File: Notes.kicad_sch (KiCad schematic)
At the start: 0 parts

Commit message: Updated notes
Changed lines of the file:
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@@
 		)
 	)
-	(text_box "POWER MANAGEMENT NOTES:\n- The input power goes through three stages \n  1. a) External Power: LM73100RPWR, 2.7 - 23 V, 5.5 A Integrated Ideal Diode with Input Reverse Polarity and Overvoltage Protection\n     b) USB POWER: SS34-E3/57T Diode\n  2. TPS259531DSGR 2.7V to 18V, 4-A, 34-mΩ eFuse With Fast Overvoltage Protection\n  3. TPS62442RQRR, 2.75-V to 6-V, Dual-Channel Step-Down Converter with Adjustable Frequency\n\n- Stage Description:\n  1. The power is sourced from the imediatelly connected power source without relying on jumpers to manual selection. The diodes prevent current from flowing back to a source in case of multiple ppower sources being conected.\n     The ideal diode was used for thhe external power source to limit power loss inherent in a regular diode as the eternal power source will at times be a battery.   \n     The ideal diode includes ppolarity protection (not required on the USB sources)\n  2. The eFuse provides overvoltage protection, undervoltage lockout, and limits inrussh current.\n  3. SMPS that outputs two power rails. The first is dedicated and controlled by the ESP32P4 core. The second is general 3.3V power rail used by all other components.\n"
+	(text_box "POWER MANAGEMENT NOTES:\n- The input power goes through three stages \n  1. a) External Power: LM73100RPWR, 2.7 - 23 V, 5.5 A Integrated Ideal Diode with Input Reverse Polarity and Overvoltage Protection\n     b) USB POWER: SS34-E3/57T Diode\n  2. TPS259531DSGR 2.7V to 18V, 4-A, 34-mΩ eFuse With Fast Overvoltage Protection\n  3. TPS62442RQRR, 2.75-V to 6-V, Dual-Channel Step-Down Converter with Adjustable Frequency\n\n- Stage Description:\n  1. The power is sourced from the imediatelly connected power source without relying on jumpers to manual selection. The diodes prevent current from flowing back to a source in case of multiple ppower sources being conected.\n     The ideal diode was used for thhe external power source to limit power loss inherent in a regular diode as the eternal power source will at times be a battery.   \n     The ideal diode includes ppolarity protection (not required on the USB sources)\n  2. The eFuse provides overvoltage protection, undervoltage lockout, Short Circuit Protection, and limits inrussh current.\n  3. SMPS that outputs two power rails. The first is dedicated and controlled by the ESP32P4 core. The second is general 3.3V power rail used by all other components.\n"
 		(exclude_from_sim no)
 		(at 27.305 29.845 0)

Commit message: SMA Update
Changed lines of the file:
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@@
 	(generator_version "8.0")
 	(paper "A4")
-	(text_box "INTERFACE NOTES:\n- SPI2 IOMUX, DMA\n- SPI3 GPIOMATRIX, NODMA\n- I2S1 GPIOMATRIX\n- I2S2 GPIOMATRIX\n- I2C0 GPIOMATRIX CSI and P4 to C5\n- I2C1 GPIOMATRIX External Interface\n- UART0 IOMUX DEBUG\n- UART1 IOMUX External Interface\n- UART2\n- UART3\n- UART4\n- I3C\n- PARLIO\n  - PSSI_PDCK (Parallel Data Clock) to parlio_tx_clk_pad_out\n  - PSSI_RDY (Ready / Flow Control) to \n  - PSSI_DE (Data Enable) to parlio_tx_data15_pad_out MSB\n  - PSSI_D0 through PSSI_D7 (8-bit Data Bus) to parlio_tx_data0_pad_out 0 to 7\n  Connect suitable pins to the PSSI/SPI header then setup pins with ESP32P4 signals\n- DSI (LCD)\n  - LCD Choice: CTP ST7701S FT5316 D310FPC9362 CST128 (MIPI 2 LANE)\n- SDIO\n  - HS Communication between the P4 and C5 (Slave)\n  - INT pin deddicated as interrupt from C5 to P4 (Not part of SDIO)\n\nSERIES TERMINATION\n- CSI, DSI, SDIO (near P4), UART0, UART1, NOT I2C\nSDIO\n- Array Series termination on SDIO DATA 0-3\n- Individual series termination on CLK, CMD\n- PU on the SDIO INT (Interrupt) pin (Open Drain)"
+	(text_box "CONTROLLED IMPEDANCE TRACE WIDTHS\n(Simulations done using ADS Controlled Impedance Line Designer)\n- Simulated is JLCPCB: JLC04161H-3313(Finished thickness1.56mm±10%)\n\n1. Microstrip Edge Coupled, 100 Ohm Differential Impedance, 0.35mm (center to center), 50mmm Length, f=1Ghz, Width = 0.1225 mm\n2. Coplanar Edge Coupled, 100 Ohm Differential Impedance, 0.35mm (center to center), 0.25mm Clearance, 50mmm Length, f=1Ghz, Width = 0.1354 mm\n3. USB Coplanar Edge Coupled, 90 Ohm Differential Impedance, 0.5mm (center to center), 0.25mm Clearance, 50mmm Length, f=240Mhz, Width = 0.1704 mm\n4. USB Microstrip Edge Coupled, 90 Ohm Differential Impedance, 0.5mm (center to center), 50mmm Length, f=240Mhz, Width = 0.1722 mm\n\nSMA CONNECTOR SIGNAL PIN (MIDDLE) FOOTPRINT\n- With normal 0.35 mm clearance resulted in a veryy significant signal degradation\n- I recalculated the clearance for the middle pin using ADS:\n  - Coplanar Single-Ended, Length: 5mm, Width: 1.37 mmm (width of the pin), f: 5GHz, Clearance = 0.4046 mm\n  \n\nINTERFACE NOTES:\n- SPI2 IOMUX, DMA\n- SPI3 GPIOMATRIX, NODMA\n- I2S1 GPIOMATRIX\n- I2S2 GPIOMATRIX\n- I2C0 GPIOMATRIX CSI and P4 to C5\n- I2C1 GPIOMATRIX External Interface\n- UART0 IOMUX DEBUG\n- UART1 IOMUX External Interface\n- UART2\n- UART3\n- UART4\n- I3C\n- PARLIO\n  - PSSI_PDCK (Parallel Data Clock) to parlio_tx_clk_pad_out\n  - PSSI_RDY (Ready / Flow Control) to \n  - PSSI_DE (Data Enable) to parlio_tx_data15_pad_out MSB\n  - PSSI_D0 through PSSI_D7 (8-bit Data Bus) to parlio_tx_data0_pad_out 0 to 7\n  Connect suitable pins to the PSSI/SPI header then setup pins with ESP32P4 signals\n- DSI (LCD)\n  - LCD Choice: CTP ST7701S FT5316 D310FPC9362 CST128 (MIPI 2 LANE)\n- SDIO\n  - HS Communication between the P4 and C5 (Slave)\n  - INT pin deddicated as interrupt from C5 to P4 (Not part of SDIO)\n\nSERIES TERMINATION\n- CSI, DSI, SDIO (near P4), UART0, UART1, NOT I2C\nSDIO\n- Array Series termination on SDIO DATA 0-3\n- Individual series termination on CLK, CMD\n- PU on the SDIO INT (Interrupt) pin (Open Drain)"
 		(exclude_from_sim no)
 		(at 113.03 29.464 0)

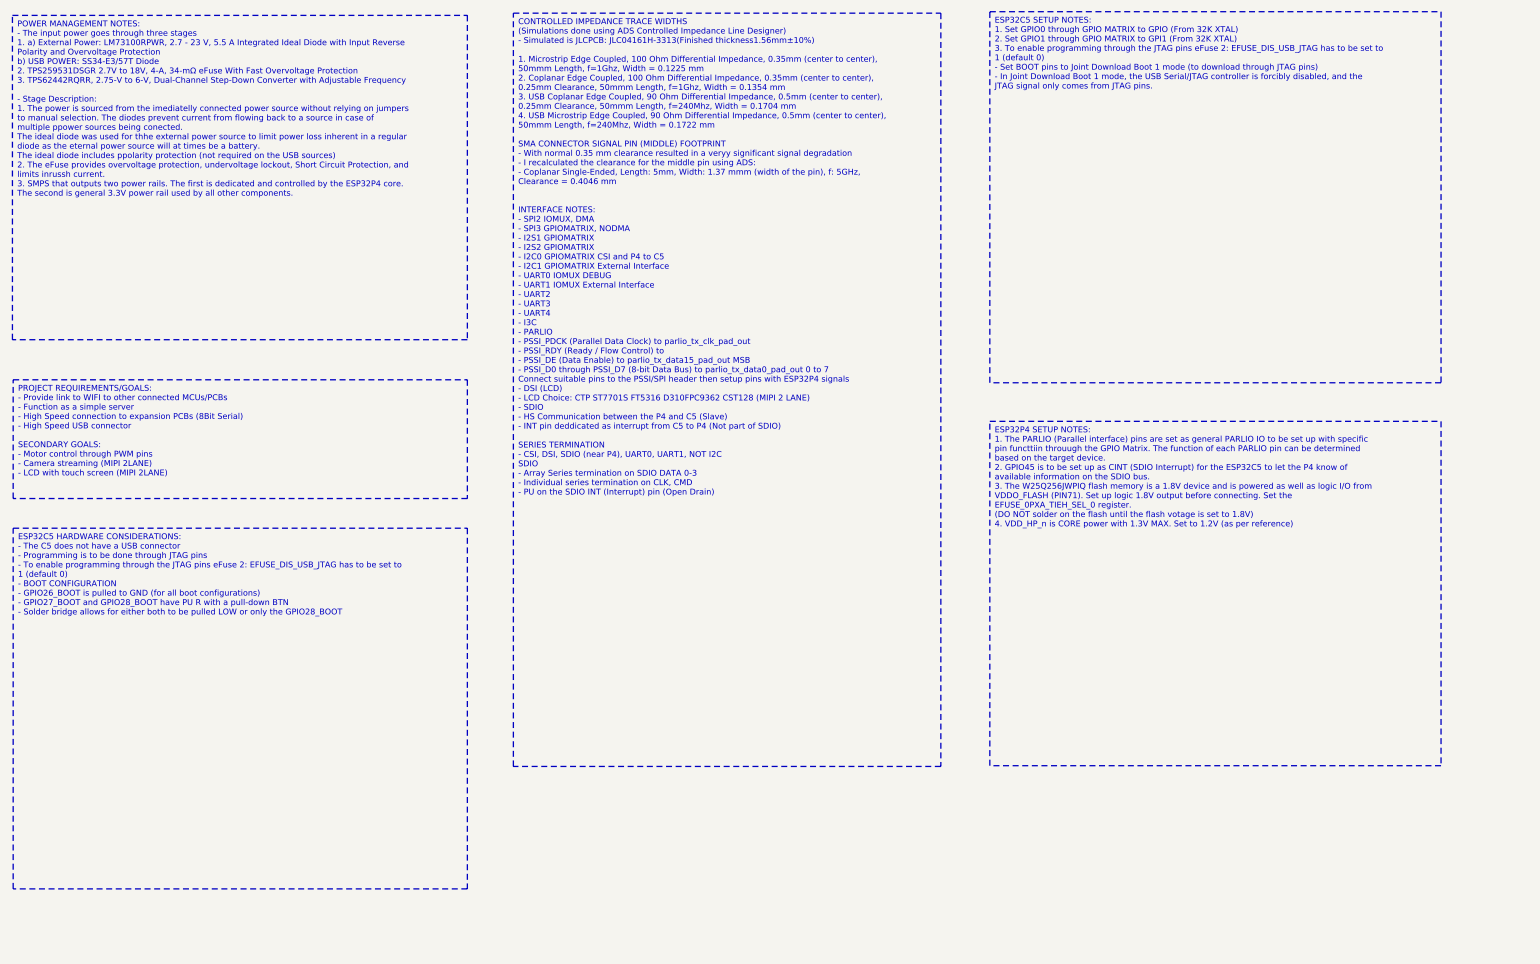
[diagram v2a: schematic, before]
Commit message: QSPI Memory Bus
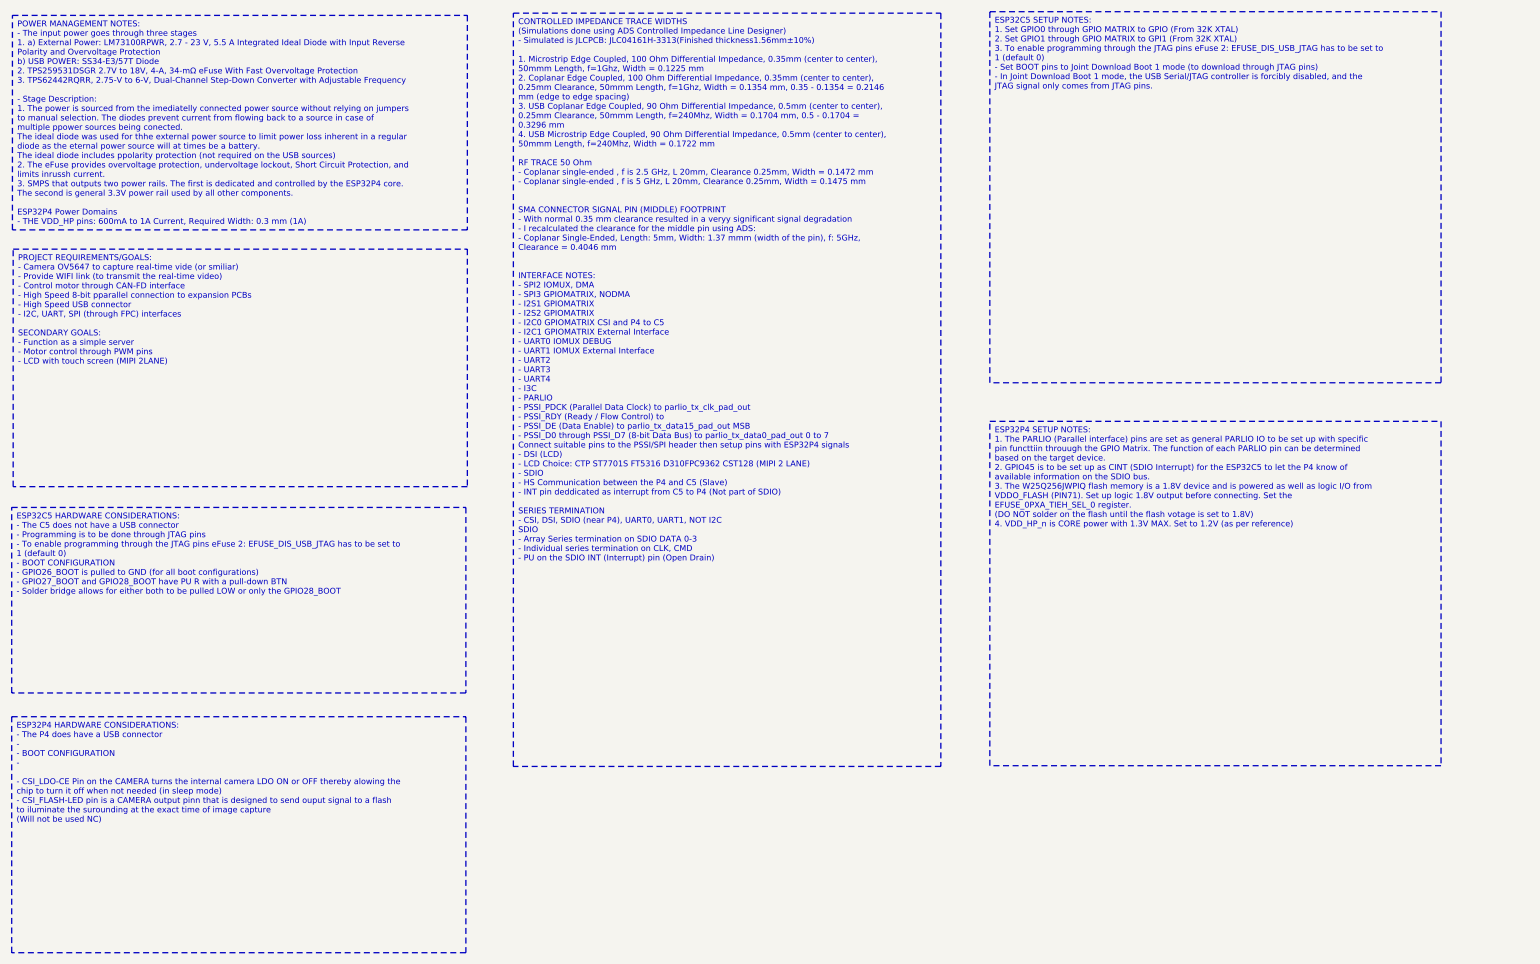
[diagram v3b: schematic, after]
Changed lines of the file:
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@@
 	(generator_version "8.0")
 	(paper "A4")
-	(text_box "CONTROLLED IMPEDANCE TRACE WIDTHS\n(Simulations done using ADS Controlled Impedance Line Designer)\n- Simulated is JLCPCB: JLC04161H-3313(Finished thickness1.56mm±10%)\n\n1. Microstrip Edge Coupled, 100 Ohm Differential Impedance, 0.35mm (center to center), 50mmm Length, f=1Ghz, Width = 0.1225 mm\n2. Coplanar Edge Coupled, 100 Ohm Differential Impedance, 0.35mm (center to center), 0.25mm Clearance, 50mmm Length, f=1Ghz, Width = 0.1354 mm\n3. USB Coplanar Edge Coupled, 90 Ohm Differential Impedance, 0.5mm (center to center), 0.25mm Clearance, 50mmm Length, f=240Mhz, Width = 0.1704 mm\n4. USB Microstrip Edge Coupled, 90 Ohm Differential Impedance, 0.5mm (center to center), 50mmm Length, f=240Mhz, Width = 0.1722 mm\n\nSMA CONNECTOR SIGNAL PIN (MIDDLE) FOOTPRINT\n- With normal 0.35 mm clearance resulted in a veryy significant signal degradation\n- I recalculated the clearance for the middle pin using ADS:\n  - Coplanar Single-Ended, Length: 5mm, Width: 1.37 mmm (width of the pin), f: 5GHz, Clearance = 0.4046 mm\n  \n\nINTERFACE NOTES:\n- SPI2 IOMUX, DMA\n- SPI3 GPIOMATRIX, NODMA\n- I2S1 GPIOMATRIX\n- I2S2 GPIOMATRIX\n- I2C0 GPIOMATRIX CSI and P4 to C5\n- I2C1 GPIOMATRIX External Interface\n- UART0 IOMUX DEBUG\n- UART1 IOMUX External Interface\n- UART2\n- UART3\n- UART4\n- I3C\n- PARLIO\n  - PSSI_PDCK (Parallel Data Clock) to parlio_tx_clk_pad_out\n  - PSSI_RDY (Ready / Flow Control) to \n  - PSSI_DE (Data Enable) to parlio_tx_data15_pad_out MSB\n  - PSSI_D0 through PSSI_D7 (8-bit Data Bus) to parlio_tx_data0_pad_out 0 to 7\n  Connect suitable pins to the PSSI/SPI header then setup pins with ESP32P4 signals\n- DSI (LCD)\n  - LCD Choice: CTP ST7701S FT5316 D310FPC9362 CST128 (MIPI 2 LANE)\n- SDIO\n  - HS Communication between the P4 and C5 (Slave)\n  - INT pin deddicated as interrupt from C5 to P4 (Not part of SDIO)\n\nSERIES TERMINATION\n- CSI, DSI, SDIO (near P4), UART0, UART1, NOT I2C\nSDIO\n- Array Series termination on SDIO DATA 0-3\n- Individual series termination on CLK, CMD\n- PU on the SDIO INT (Interrupt) pin (Open Drain)"
+	(text_box "CONTROLLED IMPEDANCE TRACE WIDTHS\n(Simulations done using ADS Controlled Impedance Line Designer)\n- Simulated is JLCPCB: JLC04161H-3313(Finished thickness1.56mm±10%)\n\n1. Microstrip Edge Coupled, 100 Ohm Differential Impedance, 0.35mm (center to center), 50mmm Length, f=1Ghz, Width = 0.1225 mm\n2. Coplanar Edge Coupled, 100 Ohm Differential Impedance, 0.35mm (center to center), 0.25mm Clearance, 50mmm Length, f=1Ghz, Width = 0.1354 mm, 0.35 - 0.1354 = 0.2146 mm (edge to edge spacing)\n3. USB Coplanar Edge Coupled, 90 Ohm Differential Impedance, 0.5mm (center to center), 0.25mm Clearance, 50mmm Length, f=240Mhz, Width = 0.1704 mm, 0.5 - 0.1704 = 0.3296 mm\n4. USB Microstrip Edge Coupled, 90 Ohm Differential Impedance, 0.5mm (center to center), 50mmm Length, f=240Mhz, Width = 0.1722 mm\n\nRF TRACE 50 Ohm\n- Coplanar single-ended , f is 2.5 GHz, L 20mm, Clearance 0.25mm, Width = 0.1472 mm\n- Coplanar single-ended , f is 5 GHz, L 20mm, Clearance 0.25mm, Width = 0.1475 mm\n\n\nSMA CONNECTOR SIGNAL PIN (MIDDLE) FOOTPRINT\n- With normal 0.35 mm clearance resulted in a veryy significant signal degradation\n- I recalculated the clearance for the middle pin using ADS:\n  - Coplanar Single-Ended, Length: 5mm, Width: 1.37 mmm (width of the pin), f: 5GHz, Clearance = 0.4046 mm\n  \n\nINTERFACE NOTES:\n- SPI2 IOMUX, DMA\n- SPI3 GPIOMATRIX, NODMA\n- I2S1 GPIOMATRIX\n- I2S2 GPIOMATRIX\n- I2C0 GPIOMATRIX CSI and P4 to C5\n- I2C1 GPIOMATRIX External Interface\n- UART0 IOMUX DEBUG\n- UART1 IOMUX External Interface\n- UART2\n- UART3\n- UART4\n- I3C\n- PARLIO\n  - PSSI_PDCK (Parallel Data Clock) to parlio_tx_clk_pad_out\n  - PSSI_RDY (Ready / Flow Control) to \n  - PSSI_DE (Data Enable) to parlio_tx_data15_pad_out MSB\n  - PSSI_D0 through PSSI_D7 (8-bit Data Bus) to parlio_tx_data0_pad_out 0 to 7\n  Connect suitable pins to the PSSI/SPI header then setup pins with ESP32P4 signals\n- DSI (LCD)\n  - LCD Choice: CTP ST7701S FT5316 D310FPC9362 CST128 (MIPI 2 LANE)\n- SDIO\n  - HS Communication between the P4 and C5 (Slave)\n  - INT pin deddicated as interrupt from C5 to P4 (Not part of SDIO)\n\nSERIES TERMINATION\n- CSI, DSI, SDIO (near P4), UART0, UART1, NOT I2C\nSDIO\n- Array Series termination on SDIO DATA 0-3\n- Individual series termination on CLK, CMD\n- PU on the SDIO INT (Interrupt) pin (Open Drain)"
 		(exclude_from_sim no)
 		(at 113.03 29.464 0)
@@
 		)
 	)
-	(text_box "POWER MANAGEMENT NOTES:\n- The input power goes through three stages \n  1. a) External Power: LM73100RPWR, 2.7 - 23 V, 5.5 A Integrated Ideal Diode with Input Reverse Polarity and Overvoltage Protection\n     b) USB POWER: SS34-E3/57T Diode\n  2. TPS259531DSGR 2.7V to 18V, 4-A, 34-mΩ eFuse With Fast Overvoltage Protection\n  3. TPS62442RQRR, 2.75-V to 6-V, Dual-Channel Step-Down Converter with Adjustable Frequency\n\n- Stage Description:\n  1. The power is sourced from the imediatelly connected power source without relying on jumpers to manual selection. The diodes prevent current from flowing back to a source in case of multiple ppower sources being conected.\n     The ideal diode was used for thhe external power source to limit power loss inherent in a regular diode as the eternal power source will at times be a battery.   \n     The ideal diode includes ppolarity protection (not required on the USB sources)\n  2. The eFuse provides overvoltage protection, undervoltage lockout, Short Circuit Protection, and limits inrussh current.\n  3. SMPS that outputs two power rails. The first is dedicated and controlled by the ESP32P4 core. The second is general 3.3V power rail used by all other components.\n"
+	(text_box "POWER MANAGEMENT NOTES:\n- The input power goes through three stages \n  1. a) External Power: LM73100RPWR, 2.7 - 23 V, 5.5 A Integrated Ideal Diode with Input Reverse Polarity and Overvoltage Protection\n     b) USB POWER: SS34-E3/57T Diode\n  2. TPS259531DSGR 2.7V to 18V, 4-A, 34-mΩ eFuse With Fast Overvoltage Protection\n  3. TPS62442RQRR, 2.75-V to 6-V, Dual-Channel Step-Down Converter with Adjustable Frequency\n\n- Stage Description:\n  1. The power is sourced from the imediatelly connected power source without relying on jumpers to manual selection. The diodes prevent current from flowing back to a source in case of multiple ppower sources being conected.\n     The ideal diode was used for thhe external power source to limit power loss inherent in a regular diode as the eternal power source will at times be a battery.   \n     The ideal diode includes ppolarity protection (not required on the USB sources)\n  2. The eFuse provides overvoltage protection, undervoltage lockout, Short Circuit Protection, and limits inrussh current.\n  3. SMPS that outputs two power rails. The first is dedicated and controlled by the ESP32P4 core. The second is general 3.3V power rail used by all other components.\n\nESP32P4 Power Domains\n- THE VDD_HP pins: 600mA to 1A Current, Required Width: 0.3 mm (1A)"
 		(exclude_from_sim no)
 		(at 27.305 29.845 0)
-		(size 77.851 55.499)
+		(size 77.851 36.703)
 		(stroke
 			(width 0)
@@
 		)
 	)
+	(text_box "ESP32P4 HARDWARE CONSIDERATIONS:\n- The P4 does have a USB connector\n  - \n- BOOT CONFIGURATION\n  - \n\n- CSI_LDO-CE Pin on the CAMERA turns the internal camera LDO ON or OFF thereby alowing the chip to turn it off when not needed (in sleep mode)\n- CSI_FLASH-LED pin is a CAMERA output pinn that is designed to send ouput signal to a flash to iluminate the surounding at the exact time of image capture\n  (Will not be used NC) "
+		(exclude_from_sim no)
+		(at 27.178 149.86 0)
+		(size 77.724 40.386)
+		(stroke
+			(width 0)
+			(type dash)
+		)
+		(fill
+			(type none)
+		)
+		(effects
+			(font
+				(size 1 1)
+			)
+			(justify left top)
+		)
+	)
 	(text_box "ESP32C5 HARDWARE CONSIDERATIONS:\n- The C5 does not have a USB connector\n  - Programming is to be done through JTAG pins\n  - To enable programming through the JTAG pins eFuse 2: EFUSE_DIS_USB_JTAG has to be set to 1 (default 0)\n- BOOT CONFIGURATION\n  - GPIO26_BOOT is pulled to GND (for all boot configurations) \n  - GPIO27_BOOT and GPIO28_BOOT have PU R with a pull-down BTN\n  - Solder bridge allows for either both to be pulled LOW or only the GPIO28_BOOT"
 		(exclude_from_sim no)
-		(at 27.432 117.602 0)
-		(size 77.724 61.722)
+		(at 27.178 114.046 0)
+		(size 77.724 31.75)
 		(stroke
 			(width 0)
@@
 		)
 	)
-	(text_box "PROJECT REQUIREMENTS/GOALS:\n- Provide link to WIFI to other connected MCUs/PCBs\n- Function as a simple server\n- High Speed connection to expansion PCBs (8Bit Serial)\n- High Speed USB connector\n\nSECONDARY GOALS:\n- Motor control through PWM pins\n- Camera streaming (MIPI 2LANE)\n- LCD with touch screen (MIPI 2LANE)\n"
+	(text_box "PROJECT REQUIREMENTS/GOALS:\n- Camera OV5647 to capture real-time vide (or smiliar)\n- Provide WIFI link (to transmit the real-time video)\n- Control motor through CAN-FD interface\n- High Speed 8-bit pparallel connection to expansion PCBs\n- High Speed USB connector\n- I2C, UART, SPI (through FPC) interfaces\n\nSECONDARY GOALS:\n- Function as a simple server\n- Motor control through PWM pins\n- LCD with touch screen (MIPI 2LANE)\n"
 		(exclude_from_sim no)
-		(at 27.432 92.202 0)
-		(size 77.724 20.32)
+		(at 27.432 69.85 0)
+		(size 77.724 40.64)
 		(stroke
 			(width 0)
